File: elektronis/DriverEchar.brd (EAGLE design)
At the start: 72.7 x 80.6 mm, 27 parts, among them IC1 7805T, IC2 L293D

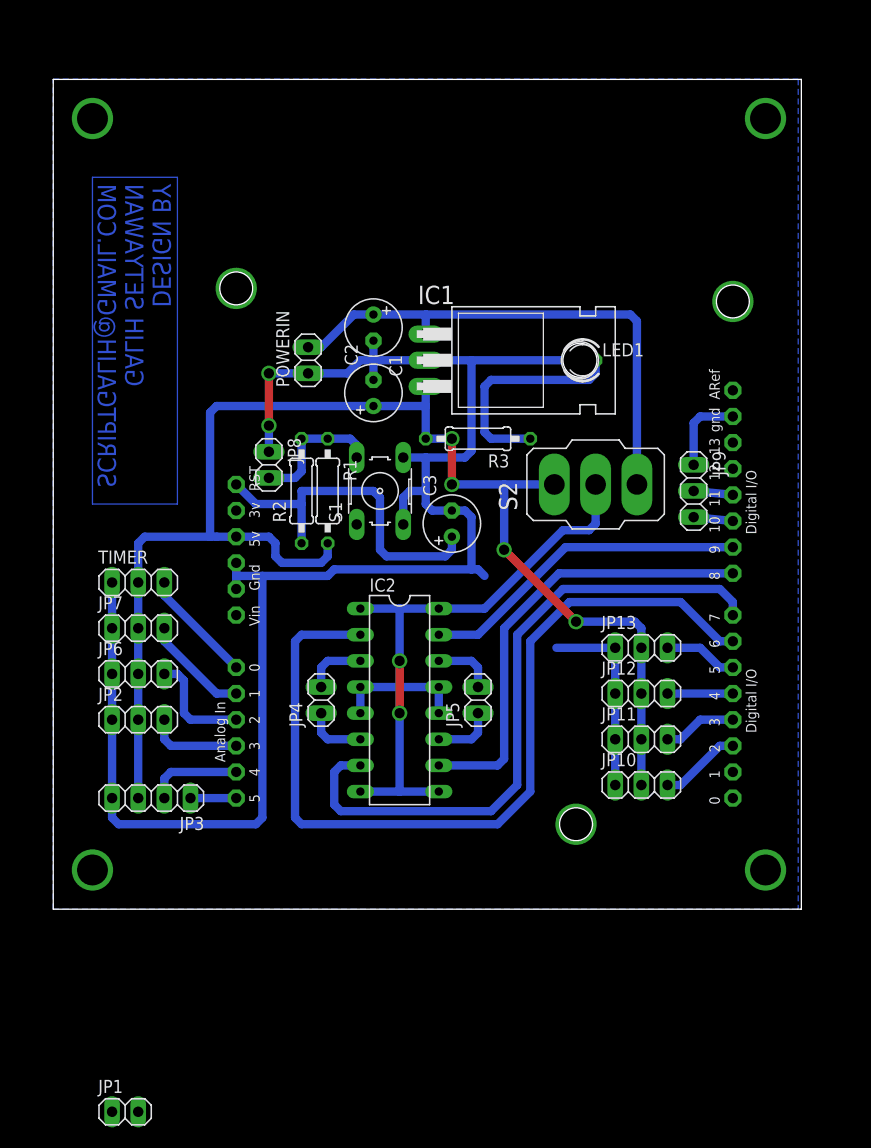
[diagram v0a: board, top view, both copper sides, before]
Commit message: update komponen
menambah tactile switch / micro switch
pembaharuan pelabelan komponen
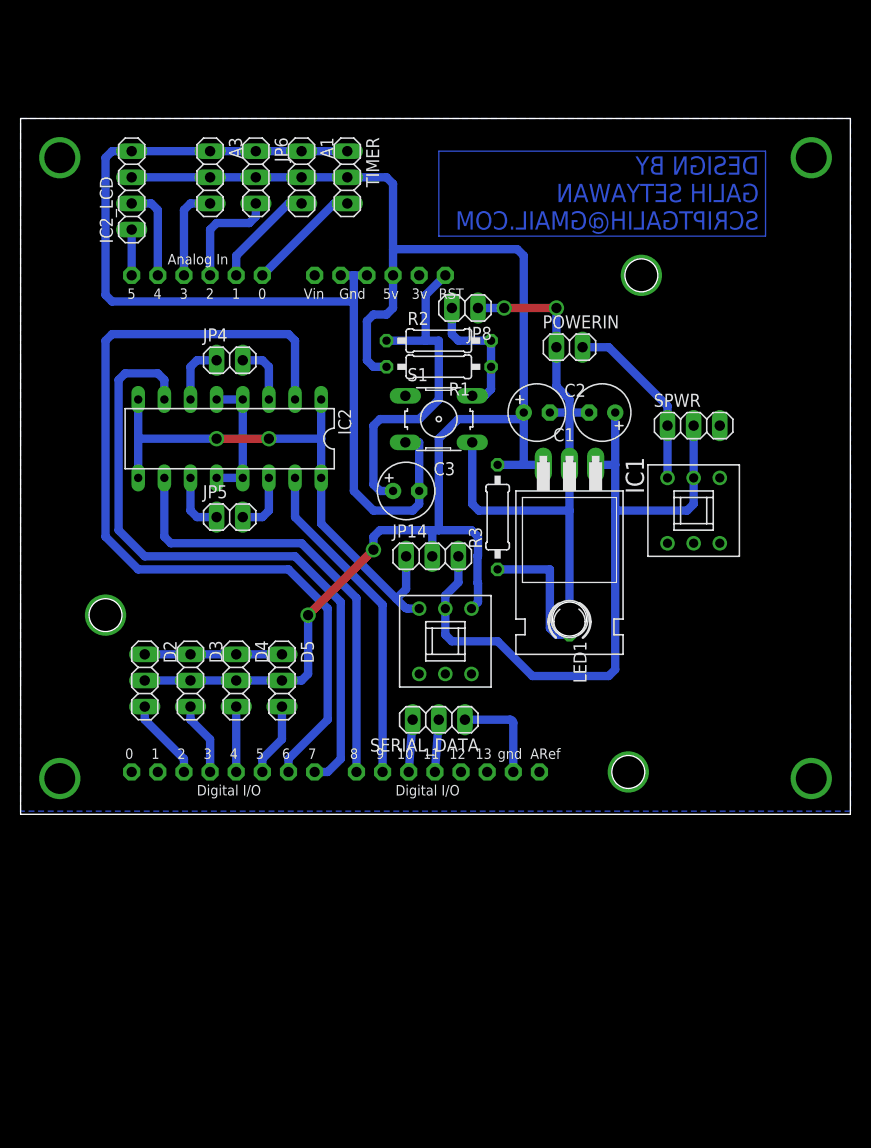
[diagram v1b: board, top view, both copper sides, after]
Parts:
- removed JP1: (no value), pinhead:1X02
- removed JP10, JP11, JP12, JP13, JP2, JP7, JP9: (no value), pinhead:1X03
- removed JP3: (no value), pinhead:1X04
- removed S2: (no value), switch:320-916
- added A1, A3, D2, D3, D4, D5, JP14, SERIAL_DATA, SPWR: (no value), pinhead:1X03
- added IC2_LCD: (no value), pinhead:1X04
- added U$2, U$3: MICROSWITCH_2X3, custom:MICROSWITCH_2X3
- moved U$1 56.8 mm to (114.3, 105.4), turned to 180 degrees
- moved JP6 49.6 mm to (62.9, 112.4), turned to 270 degrees
- moved TIMER 44.3 mm to (71.8, 112.4), turned to 270 degrees
- moved JP4 34.2 mm to (60.3, 94.6), turned to 0 degrees
- moved IC2 30.3 mm to (60.3, 87.0), turned to 180 degrees
- moved JP5 30.0 mm to (60.3, 79.4), turned to 0 degrees
- moved POWERIN 25.4 mm to (93.3, 95.9), turned to 0 degrees
- moved LED1 25.4 mm to (93.3, 69.2), turned to 270 degrees
- moved JP8 24.4 mm to (83.2, 99.7), turned to 180 degrees
- moved C1 23.7 mm to (96.5, 89.5), turned to 180 degrees
- moved IC1 20.7 mm to (93.3, 74.3), turned to 180 degrees
- moved R2 19.8 mm to (80.6, 96.5), turned to 0 degrees
- moved R1 16.2 mm to (80.6, 94.0), turned to 180 degrees
- moved C2 16.0 mm to (90.2, 89.5), turned to 0 degrees
- moved S1 9.03 mm to (80.6, 88.9), turned to 0 degrees
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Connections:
- net 5V: now also A1.2, A3.2, D2.2, D3.2, D4.2, D5.2, IC2_LCD.3, JP14.2, U$2.NC1; no longer JP10.2, JP11.2, JP12.2, JP13.2, JP2.2, JP3.3, JP7.2, S2.1
- net A1: now also A1.3; no longer JP7.3
- net A3: now also A3.3; no longer JP2.3
- net D2: now also D2.3; no longer JP10.3
- net D3: now also D3.3; no longer JP11.3
- net D4: now also D4.3; no longer JP12.3
- net D5: now also D5.3; no longer JP13.3
- net GND: now also A1.1, A3.1, D2.1, D3.1, D4.1, D5.1, IC2_LCD.4, SERIAL_DATA.1; no longer JP10.1, JP11.1, JP12.1, JP13.1, JP2.1, JP3.4, JP7.1, JP9.1
- net RX: now also SERIAL_DATA.3; no longer JP9.3
- net SCL: now also IC2_LCD.1; no longer JP3.1
- net SDA: now also IC2_LCD.2; no longer JP3.2
- net TX: now also SERIAL_DATA.2; no longer JP9.2
- net VBAT: now also JP14.3, SPWR.2, U$2.NO1, U$3.NO1; no longer POWERIN.2, S2.3
- net VIN: now also POWERIN.2, SPWR.1, U$3.C1
- net VM: now also JP14.1, U$2.C1; no longer S2.2
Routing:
- net VBAT: track 51.3 -> 69.0 mm
- net VIN: track 0.00 -> 17.6 mm
- net 5V: track 140.2 -> 155.1 mm, vias 4 -> 2
- net GND: track 192.4 -> 179.5 mm
- net N$4: track 21.7 -> 13.0 mm
- net TX: track 3.83 -> 5.09 mm
- net RX: track 3.83 -> 5.09 mm
- net RST: track 34.0 -> 33.2 mm
- net VM: track 55.5 -> 54.9 mm
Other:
- board size 72.7 x 80.6 mm -> 80.6 x 67.6 mm

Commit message: fix jumper and pin header space
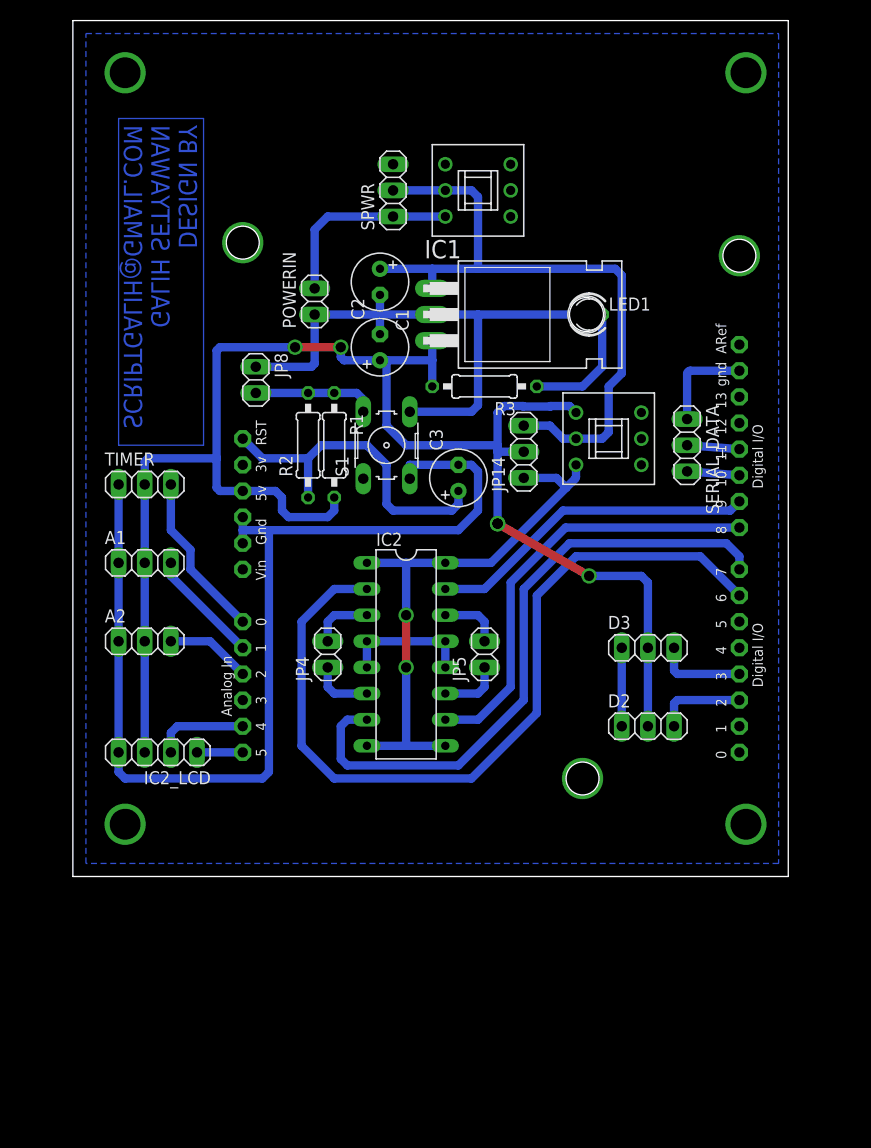
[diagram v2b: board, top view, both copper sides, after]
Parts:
- removed A3, D4, D5, JP6: (no value), pinhead:1X03
- added A2: (no value), pinhead:1X03
- moved U$1 57.1 mm to (59.1, 120.0), turned to 270 degrees
- moved IC2_LCD 54.7 mm to (53.3, 56.5), turned to 180 degrees
- moved D2 49.1 mm to (101.0, 59.1), turned to 0 degrees
- moved D3 44.6 mm to (101.0, 66.7), turned to 0 degrees
- moved A1 40.4 mm to (52.1, 74.9), turned to 0 degrees
- moved SPWR 37.1 mm to (76.2, 111.1), turned to 90 degrees
- moved SERIAL_DATA 36.0 mm to (104.8, 86.4), turned to 270 degrees
- moved TIMER 35.8 mm to (52.1, 82.5), turned to 0 degrees
- moved JP4 30.1 mm to (69.8, 66.0), turned to 90 degrees
- moved LED1 29.9 mm to (95.2, 99.1), turned to 0 degrees
- moved U$3 29.6 mm to (80.0, 106.0), turned to 0 degrees
- moved JP5 28.1 mm to (85.1, 66.0), turned to 90 degrees
- moved IC2 27.1 mm to (77.5, 66.0), turned to 270 degrees
- moved POWERIN 25.2 mm to (68.6, 100.3), turned to 90 degrees
- moved C1 25.0 mm to (74.9, 102.2), turned to 270 degrees
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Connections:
- net 5V: now also A2.2; no longer A3.2, D4.2, D5.2, JP6.2
- net A2: now also A2.3; no longer JP6.3
- net A3: no longer A3.3
- net D4: no longer D4.3
- net D5: no longer D5.3
- net GND: now also A2.1; no longer A3.1, D4.1, D5.1, JP6.1
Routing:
- net A3: track 9.15 -> 0.00 mm
- net D5: track 7.14 -> 0.00 mm
- net D4: track 6.35 -> 0.00 mm
- net A0: track 11.1 -> 16.2 mm
- net PWM1: track 85.6 -> 80.8 mm
- net 5V: track 155.1 -> 159.9 mm, vias 2 -> 5
- net VBAT: track 69.0 -> 66.0 mm
- net A2: track 10.7 -> 8.30 mm
- net EN1: track 64.3 -> 62.0 mm
- net GND: track 179.5 -> 177.5 mm, vias 2 -> 0
- net D3: track 7.14 -> 8.70 mm
- net N$2: track 13.4 -> 11.9 mm
- net EN2: track 43.7 -> 42.3 mm
- net VIN: track 17.6 -> 18.9 mm
- net A1: track 10.4 -> 11.1 mm
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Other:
- board size 80.6 x 67.6 mm -> 69.5 x 83.2 mm
